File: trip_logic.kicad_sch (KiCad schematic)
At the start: 0 parts

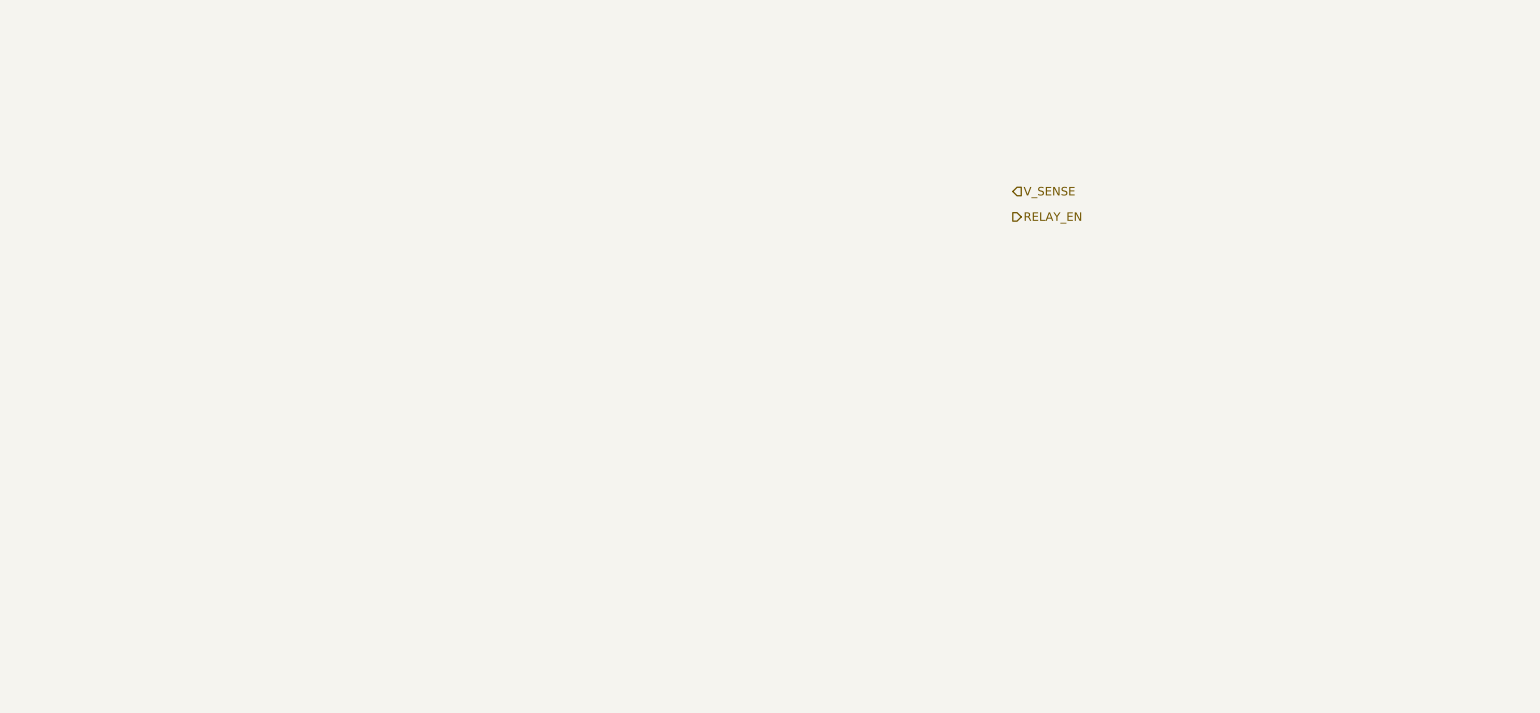
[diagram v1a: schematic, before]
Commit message: Add trip logic sheet
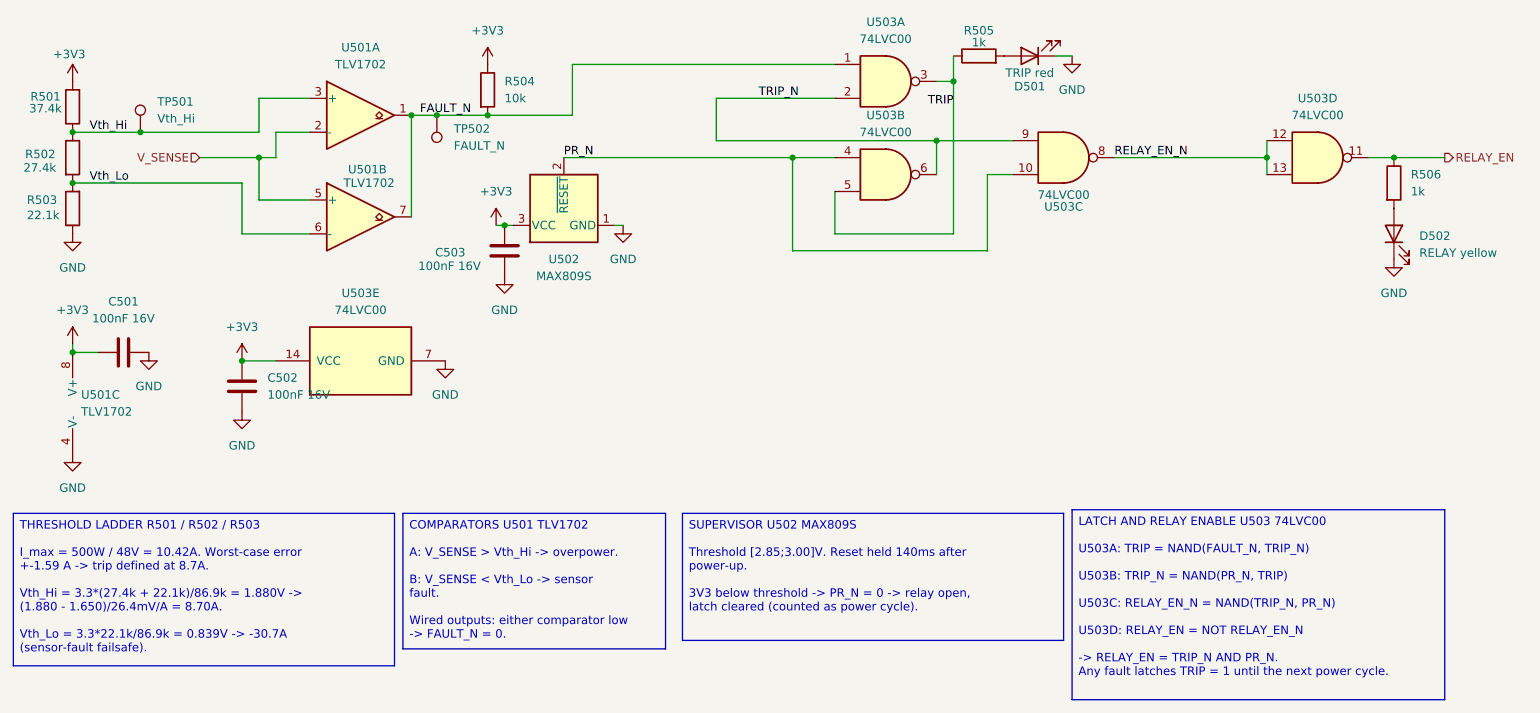
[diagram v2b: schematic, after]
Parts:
- added C501, C502, C503: 100nF 16V, Capacitor_SMD:C_0603_1608Metric, symbol Device:C
- added D501: TRIP red, LED_SMD:LED_0603_1608Metric, symbol Device:LED
- added D502: RELAY yellow, LED_SMD:LED_0603_1608Metric, symbol Device:LED
- added R501: 37.4k, Resistor_SMD:R_0603_1608Metric, symbol Device:R
- added R502: 27.4k, Resistor_SMD:R_0603_1608Metric, symbol Device:R
- added R503: 22.1k, Resistor_SMD:R_0603_1608Metric, symbol Device:R
- added R504: 10k, Resistor_SMD:R_0603_1608Metric, symbol Device:R
- added R505, R506: 1k, Resistor_SMD:R_0603_1608Metric, symbol Device:R
- added TP501: Vth_Hi, TestPoint:TestPoint_Pad_D1.5mm, symbol Connector:TestPoint
- added TP502: FAULT_N, TestPoint:TestPoint_Pad_D1.5mm, symbol Connector:TestPoint
- added U501: TLV1702, Package_SO:VSSOP-8_3x3mm_P0.65mm, symbol monitor:TLV1702
- added U502: MAX809S, Package_TO_SOT_SMD:SOT-23, symbol monitor:MAX809S
- added U503: 74LVC00, Package_SO:SOIC-14_3.9x8.7mm_P1.27mm, symbol monitor:74LVC00
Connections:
- net RELAY_EN: now also R506.1, U503.11
- net V_SENSE: now also U501.2 (-), U501.5 (+)
- new net: D501.2 (A), R505.2
- new net: D502.2 (A), R506.2
- new net +3V3: C501.1, C502.1, C503.2, R501.2, R504.1, U501.8 (V+), U502.3 (VCC), U503.14 (VCC)
- new net FAULT_N: R504.2, TP502.1, U501.1, U501.7, U503.1
- new net GND: C501.2, C502.2, C503.1, D501.1 (K), D502.1 (K), R503.1, U501.4 (V-), U502.1 (GND), U503.7 (GND)
- new net PR_N: U502.2 (~{RESET}), U503.10, U503.4
- new net RELAY_EN_N: U503.12, U503.13, U503.8
- new net TRIP: R505.1, U503.3, U503.5
- new net TRIP_N: U503.2, U503.6, U503.9
- new net Vth_Hi: R501.1, R502.1, TP501.1, U501.3 (+)
- new net Vth_Lo: R502.2, R503.2, U501.6 (-)

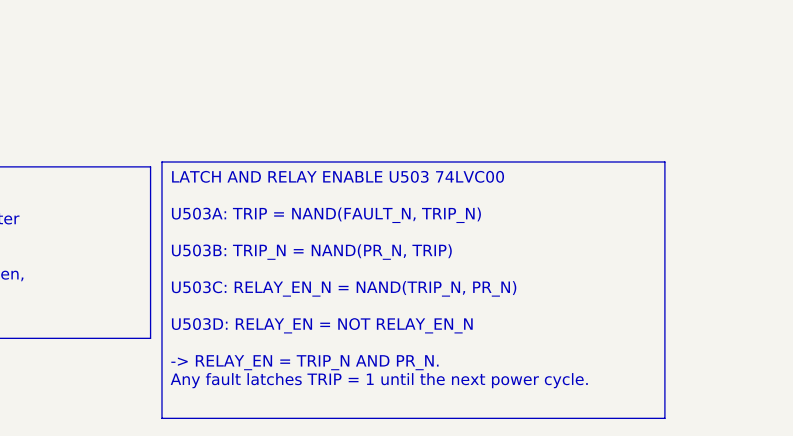
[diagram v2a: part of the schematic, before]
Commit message: Add relay sheet
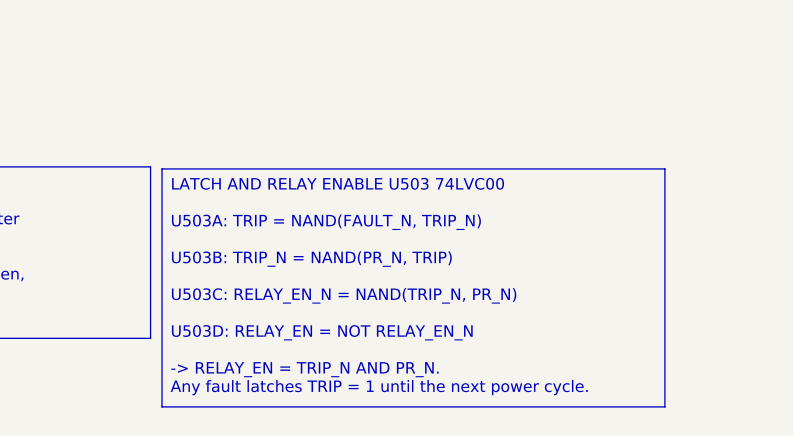
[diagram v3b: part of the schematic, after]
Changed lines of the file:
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@@
 	(text_box "LATCH AND RELAY ENABLE U503 74LVC00\n\nU503A: TRIP = NAND(FAULT_N, TRIP_N)\n\nU503B: TRIP_N = NAND(PR_N, TRIP)\n\nU503C: RELAY_EN_N = NAND(TRIP_N, PR_N)\n\nU503D: RELAY_EN = NOT RELAY_EN_N\n\n-> RELAY_EN = TRIP_N AND PR_N. \nAny fault latches TRIP = 1 until the next power cycle.\n"
 		(exclude_from_sim no)
-		(at 173.99 85.8162 0)
-		(size 55.88 28.4838)
+		(at 173.99 86.5908 0)
+		(size 55.88 26.4392)
 		(margins 0.9525 0.9525 0.9525 0.9525)
 		(stroke
